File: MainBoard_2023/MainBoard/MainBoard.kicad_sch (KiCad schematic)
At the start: 53 parts, among them J1 USB PD, J2 Conn_01x03, J3 Conn_01x02, J4 Micro_SD_Card_Det_Hirose_DM3AT, J5 Micro_SD_Card_Det_Hirose_DM3AT, Q1 AO3400A, U1 ICP-10111, U2 IP2721D, U3 BNO055, U4 XIAO, U5 Pi Pico 0, U6 Pi Pico 1

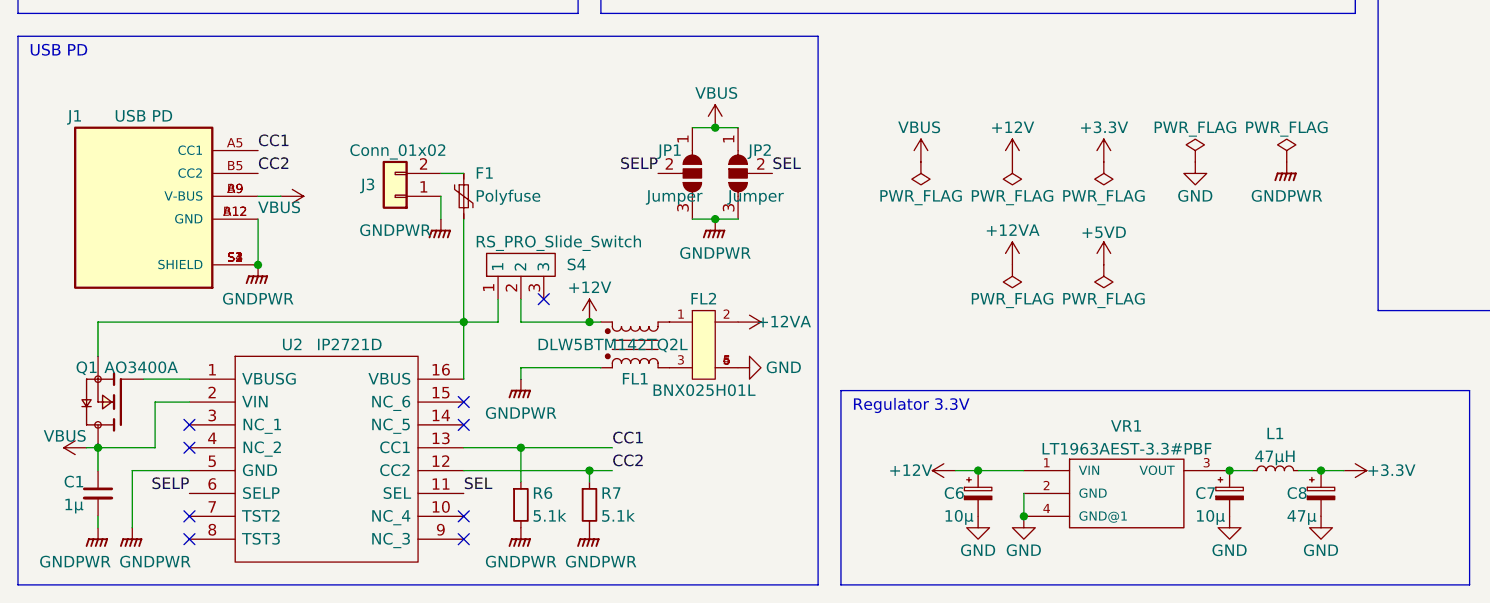
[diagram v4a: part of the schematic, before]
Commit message: アンプのGNDをGNDAに変更
GNDAとGNDをブロックタイプエミフィルとコモンモードチョークでアイソレート
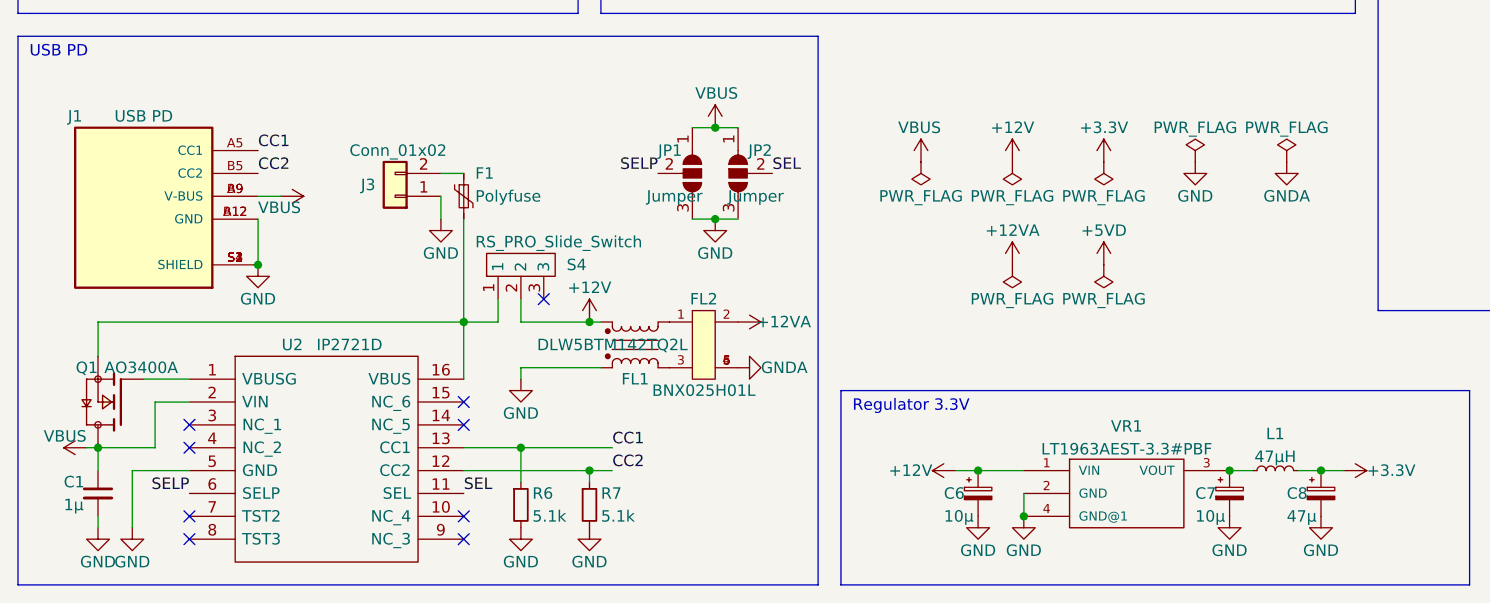
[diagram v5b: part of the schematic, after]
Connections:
- net GNDPWR is gone; now on net GND: C1.2, FL1.4, J1.A12 (GND), J1.B12 (GND), J1.S1 (SHIELD), J1.S2 (SHIELD), J1.S3 (SHIELD), J1.S4 (SHIELD), J3.1 (Pin_1), JP1.3 (B), JP2.3 (B), R6.2, R7.2, U2.5 (GND)
- net GND: no longer FL2.4, FL2.5, FL2.6
- new net GNDA: FL2.4, FL2.5, FL2.6

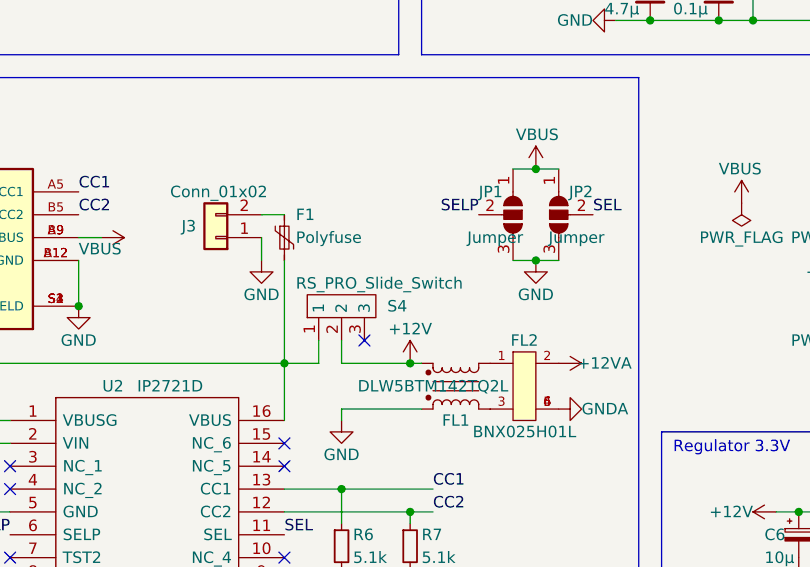
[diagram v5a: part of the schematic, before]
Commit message: 配線ちょっとだけ、電源回路の一部をベタにしたい
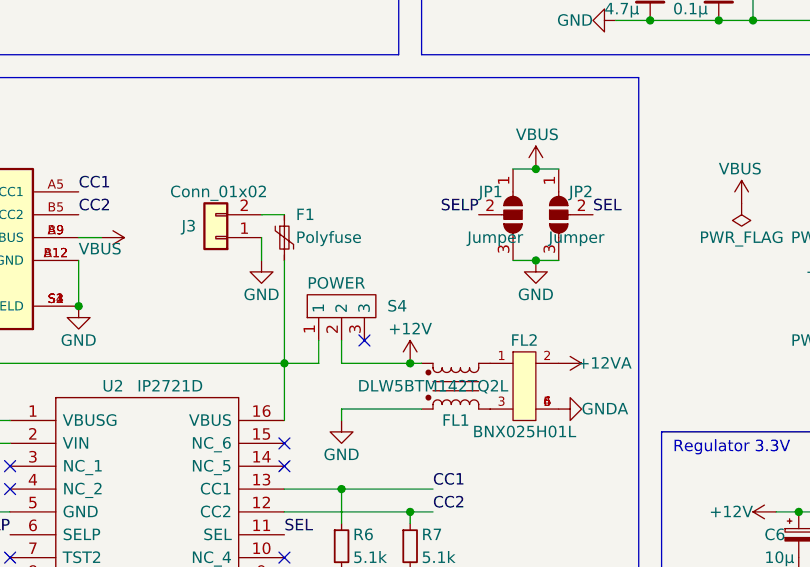
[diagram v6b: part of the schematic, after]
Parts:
- S4: value RS_PRO_Slide_Switch -> POWER
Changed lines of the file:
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@@
       (effects (font (size 1.27 1.27)) (justify left))
     )
-    (property "Value" "RS_PRO_Slide_Switch" (id 1) (at 64.77 156.21 0)
+    (property "Value" "POWER" (id 1) (at 66.04 156.21 0)
       (effects (font (size 1.27 1.27)) (justify left))
     )
@@
     )
     (path "/2ba53bb7-1045-4441-bf07-c007c131b968"
-      (reference "S4") (unit 1) (value "RS_PRO_Slide_Switch") (footprint "RS_PRO_PCB_Slide_Switch_SPDT_Latching_3A_120V_ac_Top:RS_PRO_PCB_Slide_Switch_SPDT_Latching_3A_120V_ac_Top")
+      (reference "S4") (unit 1) (value "POWER") (footprint "RS_PRO_PCB_Slide_Switch_SPDT_Latching_3A_120V_ac_Top:RS_PRO_PCB_Slide_Switch_SPDT_Latching_3A_120V_ac_Top")
     )
     (path "/6a473b76-9def-47b1-bd12-ebbe49093892/a0abd0b9-06e2-4001-8134-c9815ffb8734"
